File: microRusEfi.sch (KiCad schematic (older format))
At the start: 40 parts, among them J4 Conn_02x05_Counter_Clockwise, J5 Conn_01x04_Male, J6 Conn_01x05_Female, U3 Molex_48_pin, U7 XC6206 3.3V

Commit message: Fixed rescue lib issue.
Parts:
- LOGO2: symbol microRusEfi-rescue:LOGO-rusefi_Logo -> rusefi_Logo:LOGO
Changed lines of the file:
@@
 EESchema Schematic File Version 4
-LIBS:microRusEfi-cache
 EELAYER 30 0
 EELAYER END
@@
 Ign3
 $Comp
-L microRusEfi-rescue:LOGO-rusefi_Logo LOGO2
+L rusefi_Logo:LOGO LOGO2
 U 1 1 5D54AA23
 P 11425 10225

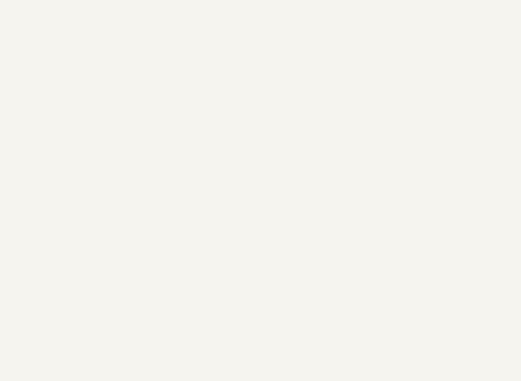
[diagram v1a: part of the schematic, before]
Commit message: Added solder-able mounting points M1 to M4.
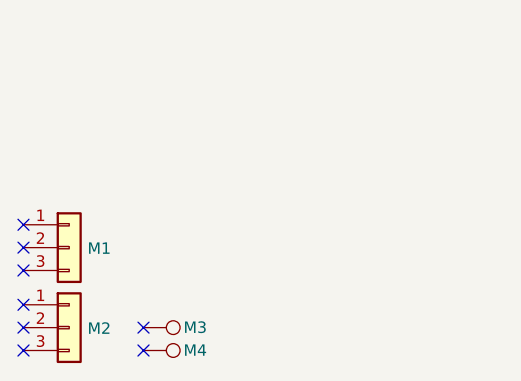
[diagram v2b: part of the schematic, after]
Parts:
- added M1, M2: Conn_01x03, Connector_PinHeader_2.54mm:PinHeader_1x03_P2.54mm_Vertical, symbol Connector_Generic:Conn_01x03
- added M3, M4: LIN, Connector_PinHeader_2.54mm:PinHeader_1x01_P2.54mm_Vertical, symbol Connector:TestPoint
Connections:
- no-connect marks 14 -> 22
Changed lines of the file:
@@
 Sheet 1 7
 Title "microRusEfi-2L"
-Date "2019-12-30"
-Rev "R0.4.7"
+Date "2020-02-12"
+Rev "R0.4.8"
 Comp "rusEFI.com"
 Comment1 "Donald Becker"
@@
 	0    -1   -1   0
 $EndComp
+$Comp
+L Connector_Generic:Conn_01x03 M2
+U 1 1 5E6A6A86
+P 850 10300
+F 0 "M2" H 930 10296 50  0000 L CNN
+F 1 "Conn_01x03" H 930 10251 50  0001 L CNN
+F 2 "Connector_PinHeader_2.54mm:PinHeader_1x03_P2.54mm_Vertical" H 850 10300 50  0001 C CNN
+F 3 "~" H 850 10300 50  0001 C CNN
+	1    850  10300
+	1    0    0    -1
+$EndComp
+$Comp
+L Connector_Generic:Conn_01x03 M1
+U 1 1 5E6A716D
+P 850 9950
+F 0 "M1" H 930 9946 50  0000 L CNN
+F 1 "Conn_01x03" H 930 9901 50  0001 L CNN
+F 2 "Connector_PinHeader_2.54mm:PinHeader_1x03_P2.54mm_Vertical" H 850 9950 50  0001 C CNN
+F 3 "~" H 850 9950 50  0001 C CNN
+	1    850  9950
+	1    0    0    -1
+$EndComp
+NoConn ~ 650  10400
+NoConn ~ 650  10300
+NoConn ~ 650  10200
+NoConn ~ 650  10050
+NoConn ~ 650  9950
+NoConn ~ 650  9850
+$Comp
+L Connector:TestPoint M4
+U 1 1 5E6EA5F0
+P 1175 10400
+F 0 "M4" V 1175 10575 50  0000 L CNN
+F 1 "LIN" V 1175 10575 50  0001 L CNN
+F 2 "Connector_PinHeader_2.54mm:PinHeader_1x01_P2.54mm_Vertical" H 1375 10400 50  0001 C CNN
+F 3 "~" H 1375 10400 50  0001 C CNN
+F 4 "DNP" H -4975 5475 50  0001 C CNN "Part #"
+F 5 "DNP" H -4975 5475 50  0001 C CNN "VEND"
+F 6 "DNP" H -4975 5475 50  0001 C CNN "VEND#"
+F 7 "DNP" H -4975 5475 50  0001 C CNN "Manufacturer"
+	1    1175 10400
+	0    1    1    0
+$EndComp
+$Comp
+L Connector:TestPoint M3
+U 1 1 5E6EC0BE
+P 1175 10300
+F 0 "M3" V 1175 10475 50  0000 L CNN
+F 1 "LIN" V 1175 10475 50  0001 L CNN
+F 2 "Connector_PinHeader_2.54mm:PinHeader_1x01_P2.54mm_Vertical" H 1375 10300 50  0001 C CNN
+F 3 "~" H 1375 10300 50  0001 C CNN
+F 4 "DNP" H -4975 5375 50  0001 C CNN "Part #"
+F 5 "DNP" H -4975 5375 50  0001 C CNN "VEND"
+F 6 "DNP" H -4975 5375 50  0001 C CNN "VEND#"
+F 7 "DNP" H -4975 5375 50  0001 C CNN "Manufacturer"
+	1    1175 10300
+	0    1    1    0
+$EndComp
+NoConn ~ 1175 10400
+NoConn ~ 1175 10300
 $EndSCHEMATC

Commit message: Added J8
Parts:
- added J8: Conn_02x05_Counter_Clockwise, Connector_PinHeader_2.54mm:PinHeader_2x05_P2.54mm_Vertical, symbol Connector_Generic:Conn_02x05_Odd_Even
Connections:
- net 12V_MREL: now also J8.2 (Pin_2)
- net 5V: now also J8.1 (Pin_1)
- net GND: now also J8.9 (Pin_9)
- net PA15: now also J8.7 (Pin_7)
- net PB8: now also J8.3 (Pin_3)
- net PB9: now also J8.6 (Pin_6)
- net PC10: now also J8.8 (Pin_8)
- net PC11: now also J8.5 (Pin_5)
- net PC12: now also J8.10 (Pin_10)
- net VDD: now also J8.4 (Pin_4)
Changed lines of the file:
@@
 NoConn ~ 1175 10400
 NoConn ~ 1175 10300
+$Comp
+L Connector_Generic:Conn_02x05_Odd_Even J8
+U 1 1 5E7157B9
+P 13100 1325
+F 0 "J8" H 13150 1775 50  0000 C CNN
+F 1 "Conn_02x05_Counter_Clockwise" H 13150 1675 50  0001 C CNN
+F 2 "Connector_PinHeader_2.54mm:PinHeader_2x05_P2.54mm_Vertical" H 13100 1325 50  0001 C CNN
+F 3 "~" H 13100 1325 50  0001 C CNN
+	1    13100 1325
+	1    0    0    -1
+$EndComp
+Text Label 13400 1325 0    50   ~ 0
+PB9
+Text Label 13400 1525 0    50   ~ 0
+PC12
+Text Label 12900 1325 2    50   ~ 0
+PC11
+Text Label 13400 1425 0    50   ~ 0
+PC10
+Text Label 12900 1125 2    60   ~ 0
+5V
+Text Label 13400 1125 0    60   ~ 0
+12V_MREL
+Text Label 13400 1225 0    60   ~ 0
+VDD
+Text Label 12900 1425 2    50   ~ 0
+PA15
+Text Label 12900 1225 2    50   ~ 0
+PB8
+Text Label 12900 1525 2    60   ~ 0
+GND
 $EndSCHEMATC

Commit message: R0.4.8 Changed to MRE connector lib.
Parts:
- removed J6: Conn_01x05_Female, Connector_PinHeader_2.54mm:PinHeader_1x05_P2.54mm_Vertical, symbol Connector:Conn_01x05_Female
- removed J8: Conn_02x05_Counter_Clockwise, Connector_PinHeader_2.54mm:PinHeader_2x05_P2.54mm_Vertical, symbol Connector_Generic:Conn_02x05_Odd_Even
- removed LIN1, M3, M4: LIN, Connector_PinHeader_2.54mm:PinHeader_1x01_P2.54mm_Vertical, symbol Connector:TestPoint
- removed M1, M2: Conn_01x03, Connector_PinHeader_2.54mm:PinHeader_1x03_P2.54mm_Vertical, symbol Connector_Generic:Conn_01x03
- added unit 2 of U3
- U3: value Molex_48_pin -> molex_48pin_MRE; footprint rusefi_lib:Molex_48 -> rusefi_lib:Molex_48_MRE; symbol rusefi_molex48:molex_48pin -> rusefi_Molex_MRE_Connector:molex_48pin_MRE
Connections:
- net 12V_SAFE: now also U3.M71, U3.M72, U3.M73
- net TLE8888-1QK/OUT_14: now also U3.J61
- net TLE8888-1QK/OUT_15: now also U3.J62
- net TLE8888-1QK/OUT_16: now also U3.J63
- net TLE8888-1QK/OUT_17: now also U3.J64
- net TLE8888-1QK/OUT_18: now also U3.J65
- no-connect marks 22 -> 28
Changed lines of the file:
@@
 INJECTOR-4
 $Comp
-L rusefi_molex48:molex_48pin U3
+L rusefi_Molex_MRE_Connector:molex_48pin_MRE U3
 U 1 1 5DD8BB43
 P 7750 2125
 F 0 "U3" V 9037 2530 60  0000 C CNN
-F 1 "Molex_48_pin" V 8931 2530 60  0000 C CNN
-F 2 "rusefi_lib:Molex_48" H 7750 2125 60  0001 C CNN
+F 1 "molex_48pin_MRE" V 8931 2530 60  0000 C CNN
+F 2 "rusefi_lib:Molex_48_MRE" H 7750 2125 60  0001 C CNN
 F 3 "" H 7750 2125 60  0001 C CNN
 F 4 "MOLEX" H 0   0   50  0001 C CNN "Manufacturer"
@@
 F59 "DFB11" I R 10750 4800 60
 $EndSheet
-Text Label 10750 6275 0    60   ~ 12
+Text Label 11075 6275 2    60   ~ 12
 LINBUS
 Wire Wire Line
@@
 Wire Wire Line
 	8875 7025 7950 7025
-$Comp
-L Connector:TestPoint LIN1
-U 1 1 5EB5BF5A
-P 11075 6275
-F 0 "LIN1" V 11075 6450 50  0000 L CNN
-F 1 "LIN" V 11075 6450 50  0001 L CNN
-F 2 "Connector_PinHeader_2.54mm:PinHeader_1x01_P2.54mm_Vertical" H 11275 6275 50  0001 C CNN
-F 3 "~" H 11275 6275 50  0001 C CNN
-F 4 "DNP" H 4925 1350 50  0001 C CNN "Part #"
-F 5 "DNP" H 4925 1350 50  0001 C CNN "VEND"
-F 6 "DNP" H 4925 1350 50  0001 C CNN "VEND#"
-F 7 "DNP" H 4925 1350 50  0001 C CNN "Manufacturer"
-	1    11075 6275
-	0    1    1    0
-$EndComp
 Wire Wire Line
 	10750 6275 11075 6275
@@
 Text Notes 14125 7575 0    60   ~ 12
 LIN bus termination
-$Comp
-L Connector:Conn_01x05_Female J6
-U 1 1 5E4D4F4D
-P 11075 5125
-F 0 "J6" H 11125 5200 50  0000 L CNN
-F 1 "Conn_01x05_Female" H 11125 5100 50  0000 L CNN
-F 2 "Connector_PinHeader_2.54mm:PinHeader_1x05_P2.54mm_Vertical" H 11075 5125 50  0001 C CNN
-F 3 "~" H 11075 5125 50  0001 C CNN
-	1    11075 5125
-	1    0    0    -1
-$EndComp
 Wire Wire Line
 	10750 4925 10875 4925
@@
 	0    -1   -1   0
 $EndComp
-$Comp
-L Connector_Generic:Conn_01x03 M2
-U 1 1 5E6A6A86
-P 850 10300
-F 0 "M2" H 930 10296 50  0000 L CNN
-F 1 "Conn_01x03" H 930 10251 50  0001 L CNN
-F 2 "Connector_PinHeader_2.54mm:PinHeader_1x03_P2.54mm_Vertical" H 850 10300 50  0001 C CNN
-F 3 "~" H 850 10300 50  0001 C CNN
-	1    850  10300
-	1    0    0    -1
-$EndComp
-$Comp
-L Connector_Generic:Conn_01x03 M1
-U 1 1 5E6A716D
-P 850 9950
-F 0 "M1" H 930 9946 50  0000 L CNN
-F 1 "Conn_01x03" H 930 9901 50  0001 L CNN
-F 2 "Connector_PinHeader_2.54mm:PinHeader_1x03_P2.54mm_Vertical" H 850 9950 50  0001 C CNN
-F 3 "~" H 850 9950 50  0001 C CNN
-	1    850  9950
-	1    0    0    -1
-$EndComp
-NoConn ~ 650  10400
-NoConn ~ 650  10300
-NoConn ~ 650  10200
-NoConn ~ 650  10050
-NoConn ~ 650  9950
-NoConn ~ 650  9850
-$Comp
-L Connector:TestPoint M4
-U 1 1 5E6EA5F0
-P 1175 10400
-F 0 "M4" V 1175 10575 50  0000 L CNN
-F 1 "LIN" V 1175 10575 50  0001 L CNN
-F 2 "Connector_PinHeader_2.54mm:PinHeader_1x01_P2.54mm_Vertical" H 1375 10400 50  0001 C CNN
-F 3 "~" H 1375 10400 50  0001 C CNN
-F 4 "DNP" H -4975 5475 50  0001 C CNN "Part #"
-F 5 "DNP" H -4975 5475 50  0001 C CNN "VEND"
-F 6 "DNP" H -4975 5475 50  0001 C CNN "VEND#"
-F 7 "DNP" H -4975 5475 50  0001 C CNN "Manufacturer"
-	1    1175 10400
-	0    1    1    0
-$EndComp
-$Comp
-L Connector:TestPoint M3
-U 1 1 5E6EC0BE
-P 1175 10300
-F 0 "M3" V 1175 10475 50  0000 L CNN
-F 1 "LIN" V 1175 10475 50  0001 L CNN
-F 2 "Connector_PinHeader_2.54mm:PinHeader_1x01_P2.54mm_Vertical" H 1375 10300 50  0001 C CNN
-F 3 "~" H 1375 10300 50  0001 C CNN
-F 4 "DNP" H -4975 5375 50  0001 C CNN "Part #"
-F 5 "DNP" H -4975 5375 50  0001 C CNN "VEND"
-F 6 "DNP" H -4975 5375 50  0001 C CNN "VEND#"
-F 7 "DNP" H -4975 5375 50  0001 C CNN "Manufacturer"
-	1    1175 10300
-	0    1    1    0
-$EndComp
-NoConn ~ 1175 10400
-NoConn ~ 1175 10300
-$Comp
-L Connector_Generic:Conn_02x05_Odd_Even J8
-U 1 1 5E7157B9
-P 13100 1325
-F 0 "J8" H 13150 1775 50  0000 C CNN
-F 1 "Conn_02x05_Counter_Clockwise" H 13150 1675 50  0001 C CNN
-F 2 "Connector_PinHeader_2.54mm:PinHeader_2x05_P2.54mm_Vertical" H 13100 1325 50  0001 C CNN
-F 3 "~" H 13100 1325 50  0001 C CNN
-	1    13100 1325
-	1    0    0    -1
-$EndComp
-Text Label 13400 1325 0    50   ~ 0
+NoConn ~ 4550 1075
+NoConn ~ 4550 1175
+NoConn ~ 4550 1275
+NoConn ~ 5100 1125
+NoConn ~ 9600 1125
+NoConn ~ 10150 1075
+NoConn ~ 10150 1175
+NoConn ~ 10150 1275
+NoConn ~ 9200 1125
+NoConn ~ 9200 1225
+NoConn ~ 9200 1325
+NoConn ~ 8650 1325
+NoConn ~ 8650 1225
+NoConn ~ 8650 1125
+Text Label 8100 1325 0    50   ~ 0
+12V_SAFE
+Text Label 8100 1225 0    50   ~ 0
+12V_SAFE
+Text Label 8100 1125 0    50   ~ 0
+12V_SAFE
+Text Label 6450 1125 0    50   ~ 0
+GND
+Text Label 7550 1125 0    50   ~ 0
+PB8
+Text Label 6450 1325 0    50   ~ 0
+PA15
+Text Label 7550 1325 0    50   ~ 0
+5V
+Text Label 7000 1225 0    50   ~ 0
+PC11
+Text Label 7000 1125 0    50   ~ 0
 PB9
-Text Label 13400 1525 0    50   ~ 0
+Text Label 5900 1325 0    50   ~ 0
 PC12
-Text Label 12900 1325 2    50   ~ 0
-PC11
-Text Label 13400 1425 0    50   ~ 0
+Text Label 6450 1225 0    50   ~ 0
 PC10
-Text Label 12900 1125 2    60   ~ 0
-5V
-Text Label 13400 1125 0    60   ~ 0
+Text Label 7550 1225 0    50   ~ 0
 12V_MREL
-Text Label 13400 1225 0    60   ~ 0
+Text Label 7000 1325 0    50   ~ 0
 VDD
-Text Label 12900 1425 2    50   ~ 0
-PA15
-Text Label 12900 1225 2    50   ~ 0
-PB8
-Text Label 12900 1525 2    60   ~ 0
-GND
+Text Label 5900 1125 0    50   ~ 0
+LINBUS
+$Comp
+L rusefi_Molex_MRE_Connector:molex_48pin_MRE U3
+U 2 1 5E9380F7
+P 10875 5125
+F 0 "U3" H 11075 5100 60  0000 L CNN
+F 1 "molex_48pin_MRE" V 12025 5125 60  0001 C CNN
+F 2 "rusefi_lib:Molex_48_MRE" H 10875 5125 60  0001 C CNN
+F 3 "" H 10875 5125 60  0001 C CNN
+	2    10875 5125
+	1    0    0    -1
+$EndComp
 $EndSCHEMATC

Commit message: Updated footprint
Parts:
- removed J5: Conn_01x04_Male, Connector_PinHeader_2.54mm:PinHeader_1x04_P2.54mm_Vertical, symbol Connector:Conn_01x04_Male
- added unit 4 of U3
- added unit 5 of U3
- added unit 6 of U3
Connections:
- net 12V_MREL: now also U3.J802
- net 5V: now also U3.J801
- net GND: now also U3.J809
- net LINBUS: now also U3.LIN1
- net PA15: now also U3.J807
- net PB8: now also U3.J803
- net PB9: now also U3.J806
- net PC10: now also U3.J808
- net PC11: now also U3.J805
- net PC12: now also U3.J810
- net TLE8888-1QK/IGN_OUT_1: now also U3.J51
- net TLE8888-1QK/IGN_OUT_2: now also U3.J52
- net TLE8888-1QK/IGN_OUT_3: now also U3.J53
- net TLE8888-1QK/IGN_OUT_4: now also U3.J54
- net VDD: now also U3.J804
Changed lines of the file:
@@
 Wire Wire Line
 	11200 2875 13125 2875
-$Comp
-L Connector:Conn_01x04_Male J5
-U 1 1 5E292BCB
-P 13325 2975
-F 0 "J5" H 13275 3000 50  0000 R CNN
-F 1 "Conn_01x04_Male" H 13275 2900 50  0000 R CNN
-F 2 "Connector_PinHeader_2.54mm:PinHeader_1x04_P2.54mm_Vertical" H 13325 2975 50  0001 C CNN
-F 3 "~" H 13325 2975 50  0001 C CNN
-	1    13325 2975
-	-1   0    0    -1
-$EndComp
 Wire Wire Line
 	10750 3725 11275 3725
@@
 Text Label 8100 1125 0    50   ~ 0
 12V_SAFE
-Text Label 6450 1125 0    50   ~ 0
+Text Label 12925 1525 2    50   ~ 0
 GND
-Text Label 7550 1125 0    50   ~ 0
+Text Label 12925 1225 2    50   ~ 0
 PB8
-Text Label 6450 1325 0    50   ~ 0
+Text Label 12925 1425 2    50   ~ 0
 PA15
-Text Label 7550 1325 0    50   ~ 0
+Text Label 12925 1125 2    50   ~ 0
 5V
-Text Label 7000 1225 0    50   ~ 0
+Text Label 12925 1325 2    50   ~ 0
 PC11
-Text Label 7000 1125 0    50   ~ 0
+Text Label 13325 1325 0    50   ~ 0
 PB9
-Text Label 5900 1325 0    50   ~ 0
+Text Label 13325 1525 0    50   ~ 0
 PC12
-Text Label 6450 1225 0    50   ~ 0
+Text Label 13325 1425 0    50   ~ 0
 PC10
-Text Label 7550 1225 0    50   ~ 0
+Text Label 13325 1125 0    50   ~ 0
 12V_MREL
-Text Label 7000 1325 0    50   ~ 0
+Text Label 13325 1225 0    50   ~ 0
 VDD
-Text Label 5900 1125 0    50   ~ 0
+Text Label 2775 1025 0    50   ~ 0
 LINBUS
 $Comp
@@
 	1    0    0    -1
 $EndComp
+$Comp
+L rusefi_Molex_MRE_Connector:molex_48pin_MRE U3
+U 4 1 5E7587F2
+P 12225 1325
+F 0 "U3" H 13125 1650 60  0000 C CNN
+F 1 "molex_48pin_MRE" V 13406 1730 60  0001 C CNN
+F 2 "rusefi_lib:Molex_48_MRE" H 12225 1325 60  0001 C CNN
+F 3 "" H 12225 1325 60  0001 C CNN
+F 4 "MOLEX" H 4475 -800 50  0001 C CNN "Manufacturer"
+F 5 "500762-0481" H 4475 -800 50  0001 C CNN "Part #"
+F 6 "DIGI" H 4475 -800 50  0001 C CNN "VEND"
+F 7 "WM4430-ND" H 4475 -800 50  0001 C CNN "VEND#"
+	4    12225 1325
+	1    0    0    -1
+$EndComp
+$Comp
+L rusefi_Molex_MRE_Connector:molex_48pin_MRE U3
+U 5 1 5E75ADBD
+P 2175 1025
+F 0 "U3" H 2750 1175 60  0000 C CNN
+F 1 "molex_48pin_MRE" V 3356 1430 60  0001 C CNN
+F 2 "rusefi_lib:Molex_48_MRE" H 2175 1025 60  0001 C CNN
+F 3 "" H 2175 1025 60  0001 C CNN
+F 4 "MOLEX" H -5575 -1100 50  0001 C CNN "Manufacturer"
+F 5 "500762-0481" H -5575 -1100 50  0001 C CNN "Part #"
+F 6 "DIGI" H -5575 -1100 50  0001 C CNN "VEND"
+F 7 "WM4430-ND" H -5575 -1100 50  0001 C CNN "VEND#"
+	5    2175 1025
+	1    0    0    -1
+$EndComp
+$Comp
+L rusefi_Molex_MRE_Connector:molex_48pin_MRE U3
+U 6 1 5E75E517
+P 12575 3025
+F 0 "U3" H 13225 3325 60  0000 C CNN
+F 1 "molex_48pin_MRE" V 13756 3430 60  0001 C CNN
+F 2 "rusefi_lib:Molex_48_MRE" H 12575 3025 60  0001 C CNN
+F 3 "" H 12575 3025 60  0001 C CNN
+F 4 "MOLEX" H 4825 900 50  0001 C CNN "Manufacturer"
+F 5 "500762-0481" H 4825 900 50  0001 C CNN "Part #"
+F 6 "DIGI" H 4825 900 50  0001 C CNN "VEND"
+F 7 "WM4430-ND" H 4825 900 50  0001 C CNN "VEND#"
+	6    12575 3025
+	1    0    0    -1
+$EndComp

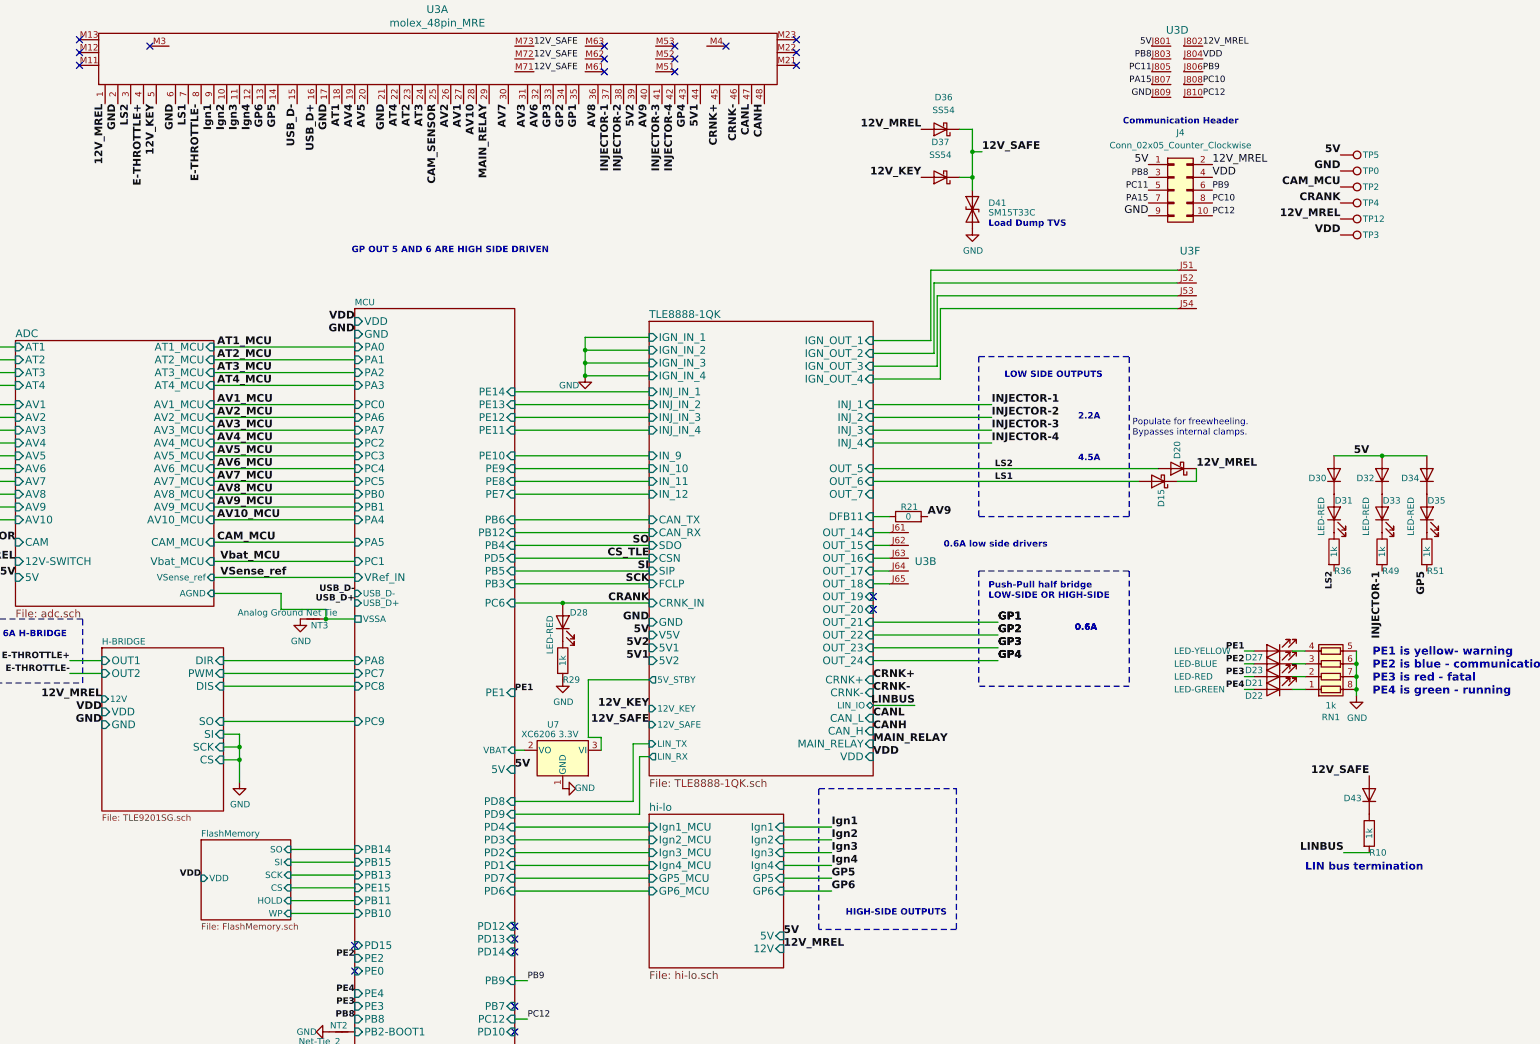
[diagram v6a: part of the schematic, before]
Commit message: Removed JP1 https://github.com/rusefi/hw_microRusEfi/issues/127
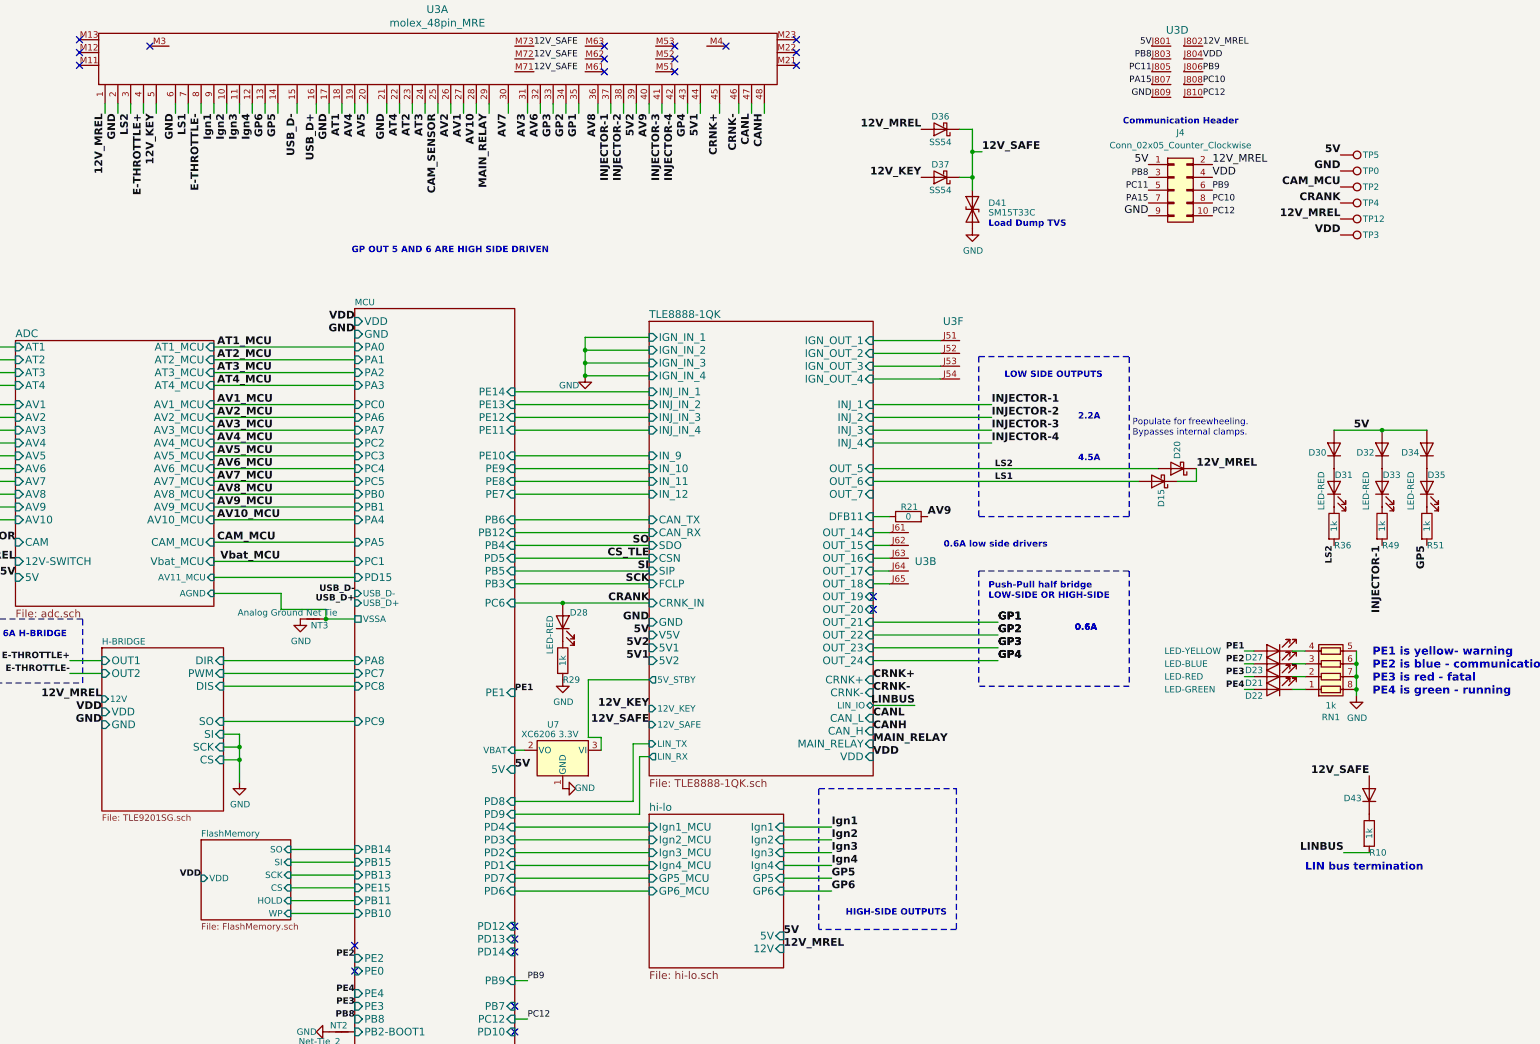
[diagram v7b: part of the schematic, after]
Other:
- moved on the sheet: D30, D31, D32, D33, D34, D35, R36, R49, R51, U3F
